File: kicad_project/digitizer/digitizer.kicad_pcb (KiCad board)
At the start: 2 copper layers, 93 x 71 mm, 63 parts, among them IC201 MAX3059ASA+T UPSTREAM, IC202 MAX6035AAUR50+T, IC203 MAX3059ASA+T DOWNSTREAM, IC204 MAX6043BAUT33+T, IC301 ADS1234IPWR, J201 DT15-4P (UPSTREAM), J202 DT06-4S (DOWNSTREAM), J301 Load Cell 1, J302 Load Cell 2, J303 Load Cell 3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

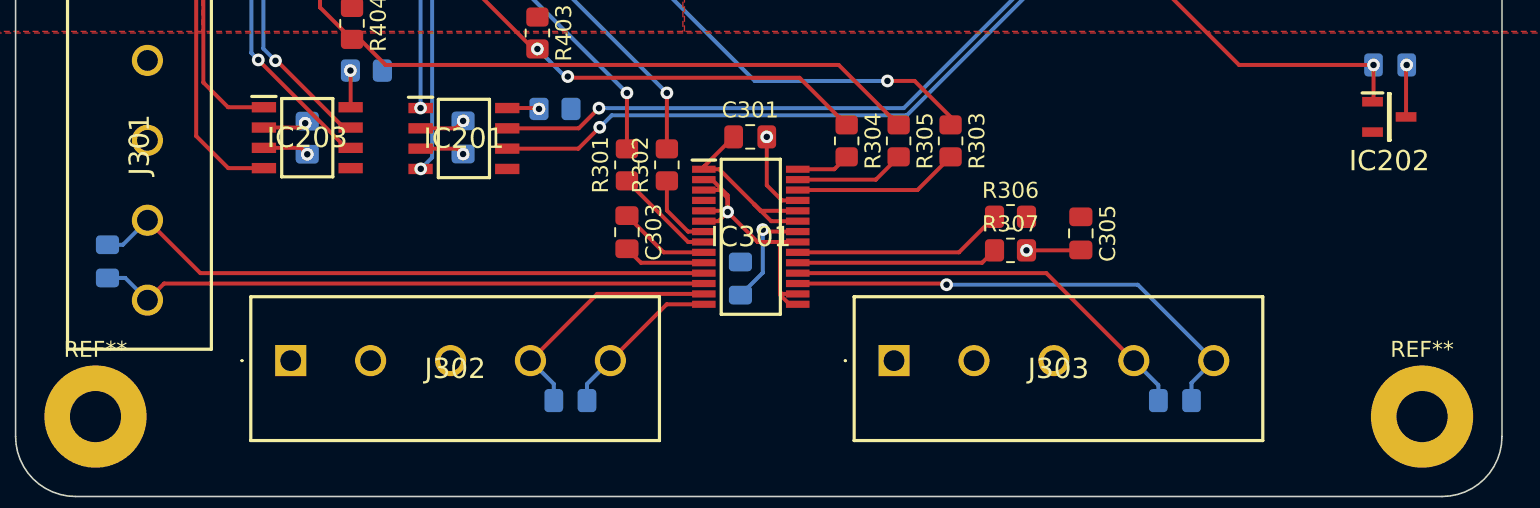
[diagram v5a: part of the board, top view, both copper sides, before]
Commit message: added 100ohm resistors to the differential analog inputs
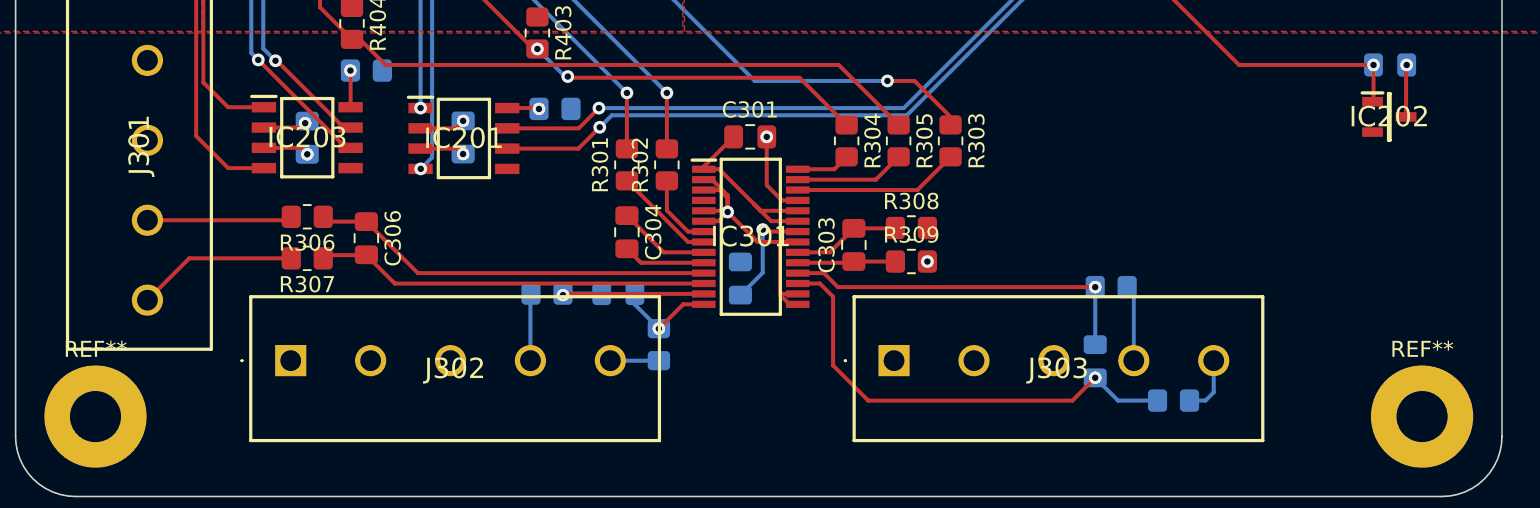
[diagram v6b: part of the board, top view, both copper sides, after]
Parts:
- added R306: 100, Resistor_SMD:R_0805_2012Metric_Pad1.20x1.40mm_HandSolder, F.Cu at (95.5, 102.5)
- added R307: 100, Resistor_SMD:R_0805_2012Metric_Pad1.20x1.40mm_HandSolder, F.Cu at (95.5, 105.1)
- added R310: 100, Resistor_SMD:R_0805_2012Metric_Pad1.20x1.40mm_HandSolder, B.Cu at (117.5, 110.5)
- added R311: 100, Resistor_SMD:R_0805_2012Metric_Pad1.20x1.40mm_HandSolder, B.Cu at (110.5, 107.3)
- added R312: 100, Resistor_SMD:R_0805_2012Metric_Pad1.20x1.40mm_HandSolder, B.Cu at (149.7, 114.0)
- added R313: 100, Resistor_SMD:R_0805_2012Metric_Pad1.20x1.40mm_HandSolder, B.Cu at (145.8, 106.9)
- C306: moved to F.Cu
- moved C306 16.3 mm to (99.2, 103.8)
- moved C303 14.2 mm to (129.7, 104.3), turned to 90 degrees
- moved C307 7.34 mm to (115.0, 107.3)
- moved R308 6.24 mm to (133.3, 103.2)
- moved R309 6.24 mm to (133.3, 105.3)
- moved C305 5.56 mm to (144.8, 111.5), turned to 90 degrees
- renumbered C305 to C303, C303 to C304, C304 to C305, R306 to R308, R307 to R309
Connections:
- C302 pad 1: 5V_CLEAN -> GND
- C302 pad 2: GND -> 5V_CLEAN
- C303 pad 1: 5V_CLEAN -> Net-(C303-Pad1)
- C303 pad 2: GND -> Net-(C303-Pad2)
- C305 pad 1: /ANALOG/load cell 3 - signal (-) -> Net-(C305-Pad1)
- C305 pad 2: /ANALOG/load cell 3 - signal (+) -> Net-(C305-Pad2)
- C306 pad 1: /ANALOG/load cell 1 - signal (+) -> Net-(C306-Pad1)
- C306 pad 2: /ANALOG/load cell 1 - signal (-) -> Net-(C306-Pad2)
- C307 pad 1: /ANALOG/load cell 2 - signal (+) -> Net-(C307-Pad1)
- C307 pad 2: /ANALOG/load cell 2 - signal (-) -> Net-(C307-Pad2)
- IC301 pad 11: /ANALOG/load cell 1 - signal (+) -> Net-(C306-Pad1)
- IC301 pad 12: /ANALOG/load cell 1 - signal (-) -> Net-(C306-Pad2)
- IC301 pad 13: /ANALOG/load cell 2 - signal (+) -> Net-(C307-Pad1)
- IC301 pad 14: /ANALOG/load cell 2 - signal (-) -> Net-(C307-Pad2)
- IC301 pad 17: /ANALOG/load cell 3 - signal (-) -> Net-(C305-Pad1)
- IC301 pad 18: /ANALOG/load cell 3 - signal (+) -> Net-(C305-Pad2)
- IC301 pad 19: Net-(IC301-Pad19) -> Net-(C303-Pad1)
- IC301 pad 20: Net-(IC301-Pad20) -> Net-(C303-Pad2)
- R308 pad 1: Net-(IC301-Pad20) -> Net-(C303-Pad2)
- R309 pad 1: Net-(IC301-Pad19) -> Net-(C303-Pad1)
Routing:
- net /ANALOG/load cell 1 - signal (+): track 39.3 -> 9.09 mm
- net Net-(C305-Pad1): track 0.00 -> 29.2 mm, vias 0 -> 1
- net /ANALOG/load cell 1 - signal (-): track 38.3 -> 10.1 mm
- net /ANALOG/load cell 3 - signal (-): track 31.1 -> 3.71 mm, vias 1 -> 0
- net Net-(C306-Pad1): track 0.00 -> 25.3 mm
- net Net-(C306-Pad2): track 0.00 -> 24.6 mm
- net Net-(C305-Pad2): track 0.00 -> 22.6 mm, vias 0 -> 1
- net /ANALOG/load cell 3 - signal (+): track 26.4 -> 4.77 mm
- net Net-(IC301-Pad20): track 13.2 -> 0.00 mm
- net Net-(IC301-Pad19): track 12.6 -> 0.00 mm
- net /ANALOG/load cell 2 - signal (+): track 15.7 -> 4.21 mm
- net Net-(C307-Pad1): track 0.00 -> 11.3 mm, vias 0 -> 1
- net /ANALOG/load cell 2 - signal (-): track 10.4 -> 3.03 mm
- net Net-(C303-Pad2): track 0.00 -> 6.74 mm
- net Net-(C307-Pad2): track 0.00 -> 6.26 mm, vias 0 -> 1
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
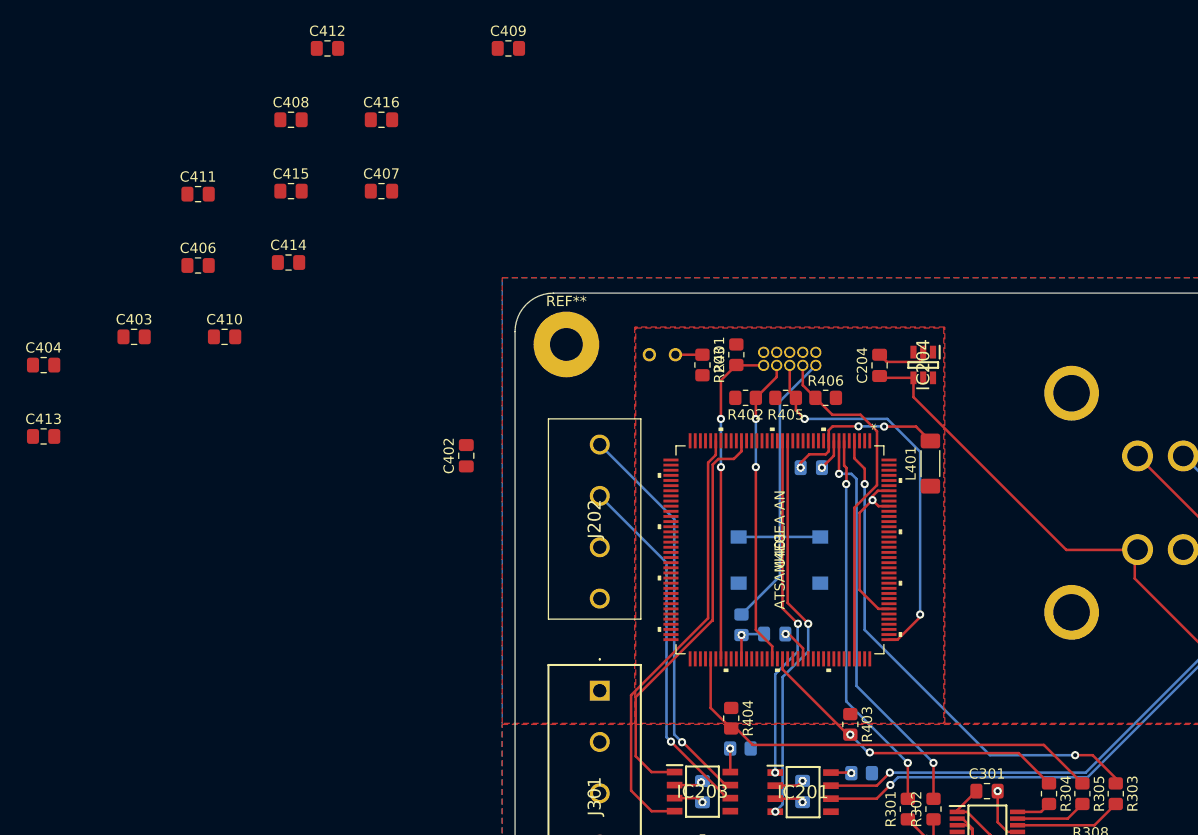
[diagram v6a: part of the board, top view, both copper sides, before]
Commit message: finished GND (i think) and VDDCORE/VDDOUT pins
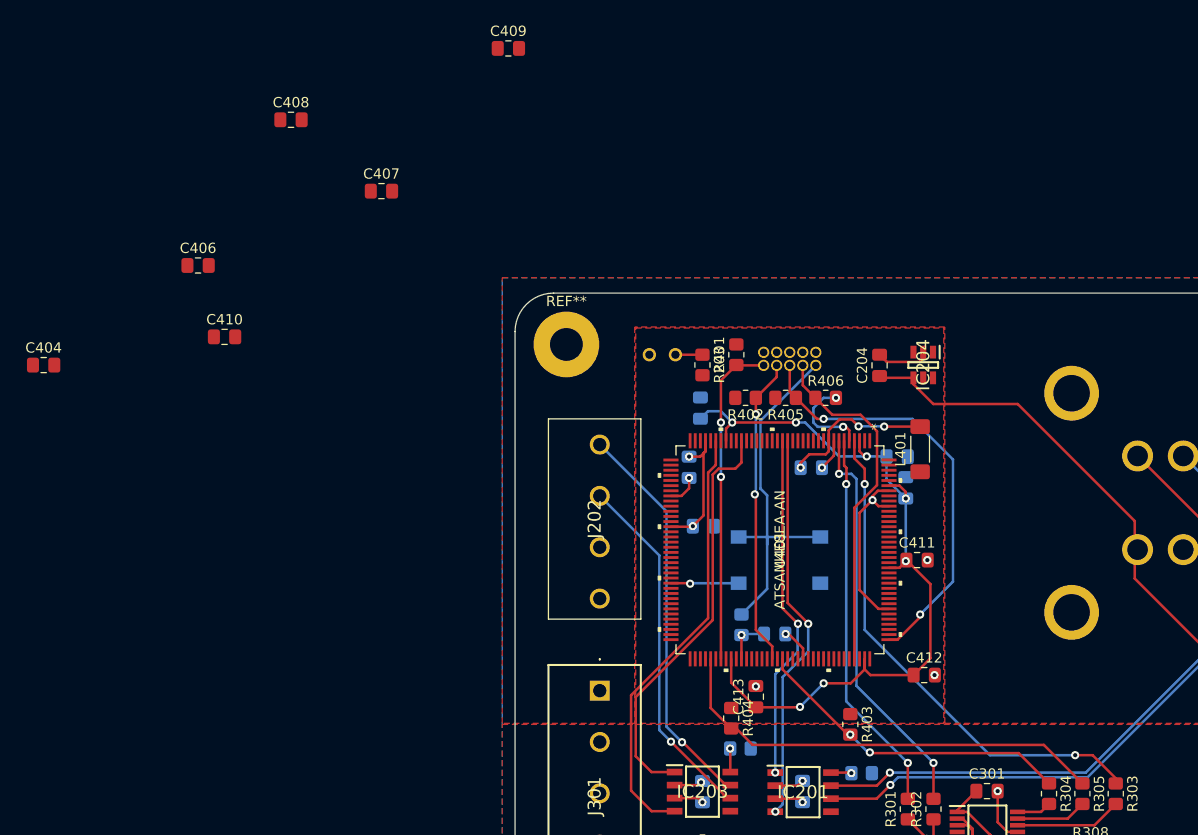
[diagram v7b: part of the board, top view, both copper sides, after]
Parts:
- C402, C403, C414, C415, C416: moved to B.Cu
- moved C412 84.3 mm to (117.1, 86.2)
- moved C411 78.6 mm to (116.4, 75.0)
- moved C403 75.2 mm to (114.5, 64.9)
- moved C413 73.8 mm to (100.7, 88.3), turned to 90 degrees
- moved C414 47.9 mm to (95.6, 71.7)
- moved C415 47.2 mm to (94.2, 66.0), turned to -90 degrees
- moved C402 42.9 mm to (115.3, 68.0)
- moved C416 41.9 mm to (95.3, 60.2), turned to 90 degrees
- moved L401 1.72 mm to (116.7, 64.2)
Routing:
- net VDD_OUT: track 0.00 -> 91.3 mm, vias 0 -> 9
- net GND: track 63.1 -> 72.9 mm, vias 9 -> 14
- net 3V3_CLEAN: track 12.9 -> 21.7 mm, vias 0 -> 2
- net /MCU/TDO: track 38.4 -> 41.8 mm
- net NRESET: track 35.2 -> 36.6 mm
- net Net-(C401-Pad1): track 16.4 -> 15.3 mm
- net 12V_CLEAN: track 69.4 -> 70.3 mm

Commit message: placed all of the components!
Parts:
- C404, C406, C407, C408, C409, C410: moved to B.Cu
- moved C406 75.4 mm to (117.3, 71.9), turned to -90 degrees
- moved C408 62.2 mm to (106.0, 68.3), turned to 180 degrees
- moved C407 61.7 mm to (119.0, 67.6), turned to -90 degrees
- moved C404 60.3 mm to (90.2, 69.3), turned to -90 degrees
- moved C410 49.6 mm to (88.8, 82.9), turned to 180 degrees
- moved C409 49.2 mm to (98.9, 69.0), turned to -90 degrees
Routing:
- net 3V3_CLEAN: track 21.7 -> 46.6 mm, vias 2 -> 8
- net /CANPWR/CANH_DOWNSTREAM: track 38.7 -> 40.5 mm
- net /MCU/TDO: track 41.8 -> 43.2 mm
